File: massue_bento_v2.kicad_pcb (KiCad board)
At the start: 2 copper layers, 100 x 21 mm, 69 parts, among them K1 CONN_3, K2 CONN_3, K3 CONN_3, P1 TST, P10 CONN_1, P11 TST, P12 TST, P13 TST, P14 TST, P15 TST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

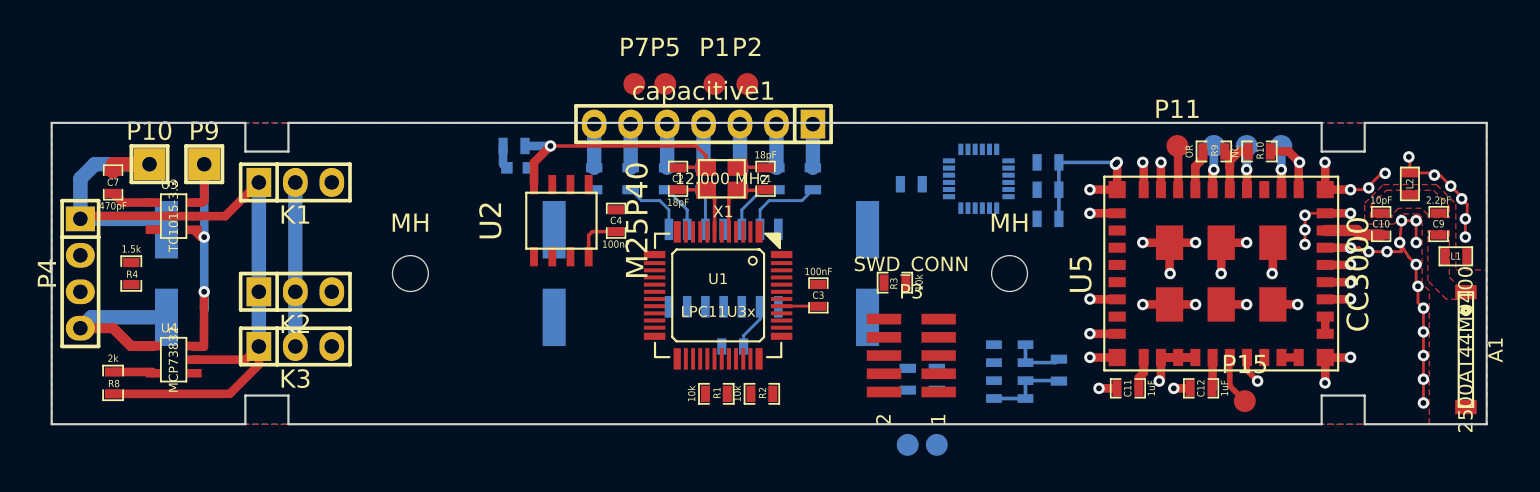
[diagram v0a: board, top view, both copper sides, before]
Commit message: New: first routing for almost all signals
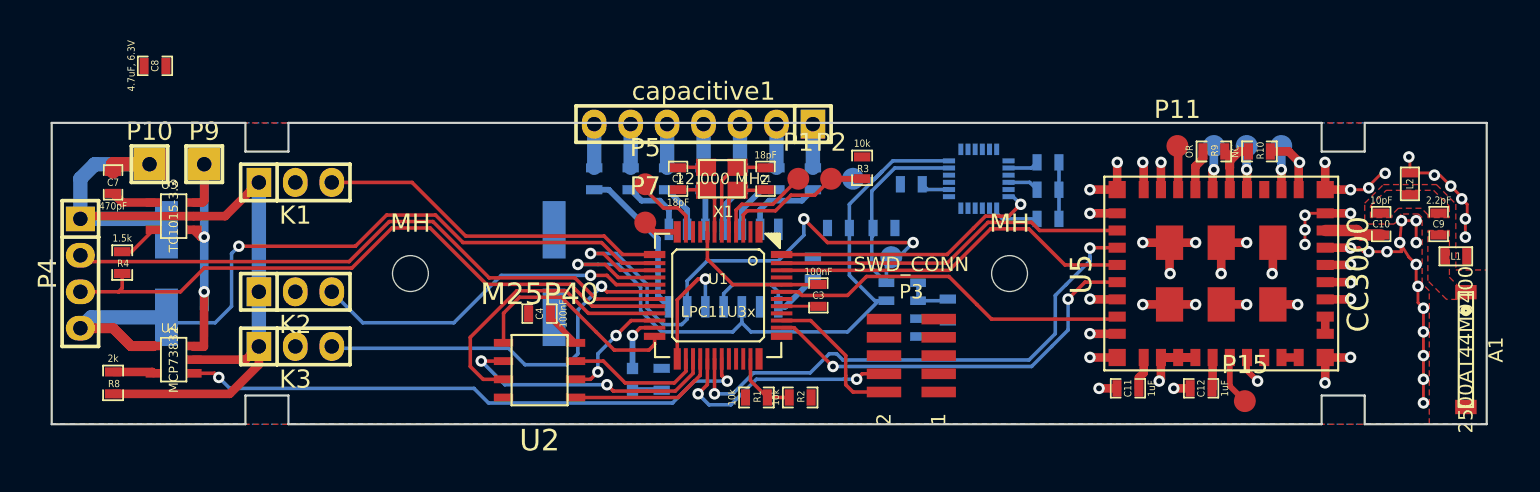
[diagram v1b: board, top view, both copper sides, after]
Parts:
- C8: value 220uF, 6.3V -> 4.7uF, 6.3V; footprint Capacitors_SMD:c_elec_8x6.7 -> SMD_Packages:SM0603_Capa; moved to F.Cu
- U7: footprint Tom:LGA -> LGA
- moved C8 51.7 mm to (106.2, 95.5), turned to 0 degrees
- moved P8 19.4 mm to (154.8, 103.4)
- moved R7 19.2 mm to (141.5, 117.4), turned to 90 degrees
- moved D1 16.8 mm to (139.5, 117.4), turned to 270 degrees
- moved P6 13.1 mm to (157.5, 108.9)
- moved R6 12.6 mm to (153.8, 106.8), turned to 0 degrees
- moved R5 10.7 mm to (157.0, 106.8), turned to 180 degrees
- moved U2 10.5 mm to (133.0, 116.7), turned to 0 degrees
- moved P7 9.68 mm to (140.4, 106.4)
- moved P1 8.82 mm to (151.0, 103.4)
- moved P2 8.82 mm to (153.3, 103.4)
- moved C18 8.81 mm to (161.4, 112.5)
- moved U8 8.65 mm to (158.3, 112.5)
- moved C4 8.39 mm to (133.0, 112.8), turned to 180 degrees
- moved R3 8.32 mm to (155.5, 102.6), turned to 270 degrees
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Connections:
- net Net-(D1-Pad1) renamed /ONBOARD_LED
- K1 pad 2: +3.3V -> VBAT
- K2 pad 2: +3.3V -> VBAT
- K3 pad 2: +3.3V -> VBAT
- U1 pad 13: /FLASH_SCK -> /LED1
- U1 pad 17: /sensors/MPU9150_INT -> /LED2
- U1 pad 18: (no net) -> /LED3
- U1 pad 21: (no net) -> /FLASH_WRITE
- U1 pad 22: (no net) -> /FLASH_SCK
- U1 pad 24: (no net) -> /FLASH_CS
- U1 pad 26: /FLASH_MISO -> /FLASH_HOLD
- U1 pad 27: /RF/CC3000_SPI_DOUT -> /FLASH_MISO
- U1 pad 28: /RF/CC3000_SPI_DIN -> /FLASH_MOSI
- U1 pad 30: /LED2 -> /RF/CC3000_SPI_DOUT
- U1 pad 31: /RF/CC3000_SPI_CLK -> /power/LIPO_CHRG_STAT
- U1 pad 32: /BATT_MON -> (no net)
- U1 pad 33: /power/LIPO_CHRG_STAT -> (no net)
- U1 pad 35: (no net) -> /BATT_MON
- U1 pad 36: /FLASH_CS -> (no net)
- U1 pad 37: /FLASH_WRITE -> (no net)
- U1 pad 38: /FLASH_MOSI -> /RF/CC3000_SPI_DIN
- U1 pad 40: /LED1 -> (no net)
- U1 pad 42: /LED3 -> (no net)
- U1 pad 43: /FLASH_HOLD -> /RF/CC3000_SPI_CLK
- U1 pad 48: (no net) -> /sensors/MPU9150_INT
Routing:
- net /sensors/SCL: track 0.00 -> 54.5 mm, vias 0 -> 3
- net /sensors/SDA: track 0.00 -> 51.4 mm, vias 0 -> 1
- net /USB_DP: track 0.00 -> 45.5 mm
- net /USB_DN: track 0.00 -> 43.6 mm
- net +5V_USB: track 15.3 -> 56.1 mm, vias 0 -> 1
- net /power/LIPO_CHRG_STAT: track 0.00 -> 40.4 mm, vias 0 -> 2
- net /RF/CC3000_SPI_DOUT: track 0.00 -> 37.2 mm, vias 0 -> 2
- net GND: track 205.6 -> 173.9 mm, vias 58 -> 56
- net /RF/CC3000_SPI_DIN: track 0.00 -> 28.2 mm, vias 0 -> 2
- net /LED3: track 0.00 -> 27.2 mm, vias 0 -> 1
- net /RF/CC3000_SPI_IRQ: track 0.00 -> 25.6 mm
- net /RF/CC3000_SPI_CLK: track 0.00 -> 25.3 mm
- net /LED2: track 0.00 -> 25.0 mm, vias 0 -> 1
- net /RF/CC3000_SPI_CS: track 0.00 -> 24.8 mm
- net /LED1: track 0.00 -> 24.6 mm
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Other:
- net class Default: clearance 0.2 -> 0.18
- net class POWER: clearance 0.3 -> 0.18
- rule trace_clearance: 0.2 -> 0.18
- board text added: "ToDo : C8 en sortie du rég 3V3"

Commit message: Finished routing of signals, re-organization of power
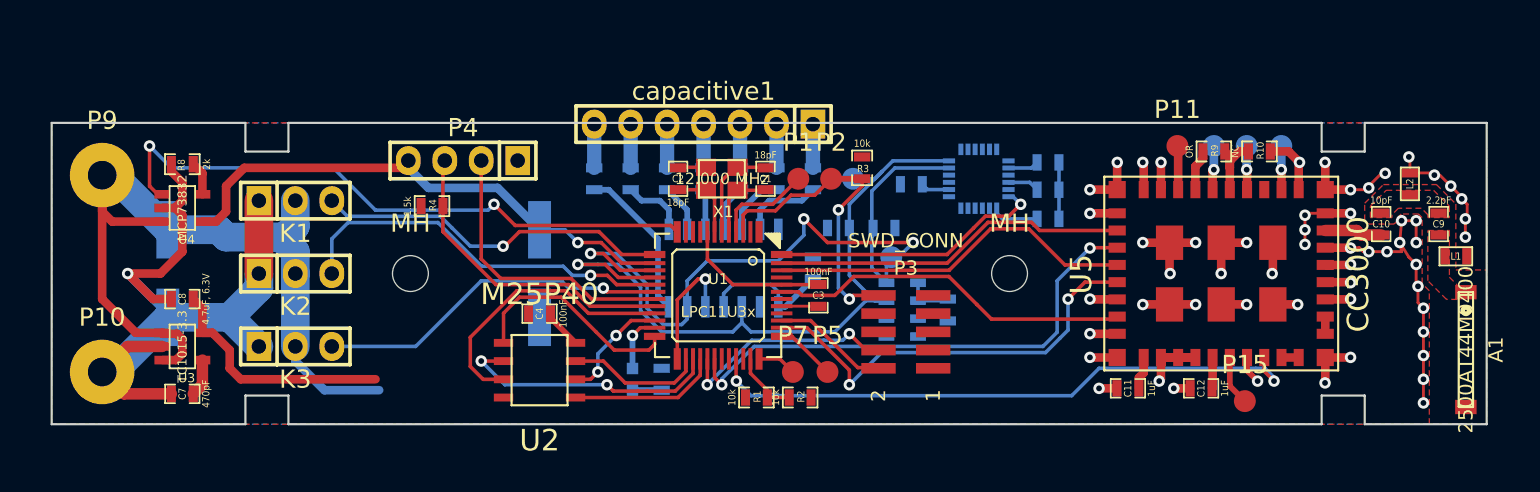
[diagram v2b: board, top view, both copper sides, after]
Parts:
- P10, P9: footprint Socket_Strips:Socket_Strip_Straight_1x01 -> Wire_Pads:SolderWirePad_single_2mmDrill
- U7: footprint LGA -> Tom:LGA
- moved P4 27.8 mm to (127.7, 102.1), turned to 0 degrees
- moved C5 26.9 mm to (107.1, 110.0), turned to 90 degrees
- moved C6 26.0 mm to (133.0, 110.0), turned to 90 degrees
- moved R4 21.9 mm to (125.5, 105.3), turned to 0 degrees
- moved P5 18.2 mm to (153.1, 116.9)
- moved C8 16.4 mm to (108.1, 111.8), turned to 180 degrees
- moved R8 16.0 mm to (108.1, 102.4), turned to 180 degrees
- moved C7 15.5 mm to (108.1, 118.4), turned to 180 degrees
- moved P10 14.8 mm to (102.5, 116.9)
- moved P7 14.6 mm to (150.7, 116.9)
- moved U4 10.6 mm to (108.1, 105.4), turned to 270 degrees
- moved U3 9.10 mm to (108.1, 115.1), turned to 270 degrees
- moved P9 7.15 mm to (102.5, 103.1)
- moved P3 1.69 mm to (158.5, 114.1)
- moved K1 1.27 mm to (116.0, 104.9)
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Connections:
- U1 pad 11: /RX -> (no net)
- U1 pad 12: /TX -> /power/LIPO_CHRG_STAT
- U1 pad 31: /power/LIPO_CHRG_STAT -> (no net)
- U1 pad 33: (no net) -> /RF/CC3000_SW_EN
- U1 pad 36: (no net) -> /TX
- U1 pad 37: (no net) -> /RX
- U1 pad 45: /RF/CC3000_SW_EN -> (no net)
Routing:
- net /RF/CC3000_SW_EN: track 0.00 -> 42.7 mm, vias 0 -> 2
- net VBAT: track 22.6 -> 62.2 mm, vias 2 -> 0
- net /USB_DP: track 45.5 -> 21.9 mm
- net /USB_DN: track 43.6 -> 20.1 mm
- net +5V_USB: track 56.1 -> 37.6 mm
- net +3.3V: track 36.4 -> 50.4 mm
- net /RESET: track 10.5 -> 22.0 mm, vias 0 -> 2
- net GND: track 173.9 -> 167.9 mm, vias 56 -> 57
- net /power/LIPO_CHRG_STAT: track 40.4 -> 43.6 mm
- net /LED3: track 27.2 -> 24.9 mm
- net /SWDIO: track 10.4 -> 8.16 mm
- net /LED2: track 25.0 -> 27.2 mm
- net /RF/CC3000_SPI_DIN: track 28.2 -> 29.8 mm
- net /RF/CC3000_SPI_DOUT: track 37.2 -> 35.9 mm
- net /SWCLK: track 16.9 -> 15.7 mm
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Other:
- board text removed: "ToDo : C8 en sortie du rég 3V3"

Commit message: new : power ehencement
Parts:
- moved P5 0.51 mm to (152.6, 116.9)
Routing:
- net GND: track 167.9 -> 332.2 mm, vias 57 -> 65
- net +3.3V: track 50.4 -> 157.0 mm, vias 0 -> 7
- net VBAT: track 62.2 -> 121.9 mm, vias 0 -> 2
- net /sensors/SCL: track 54.5 -> 53.0 mm
- net /RF/CC3000_SPI_DIN: track 29.8 -> 28.8 mm
- net /RX: track 4.22 -> 3.38 mm

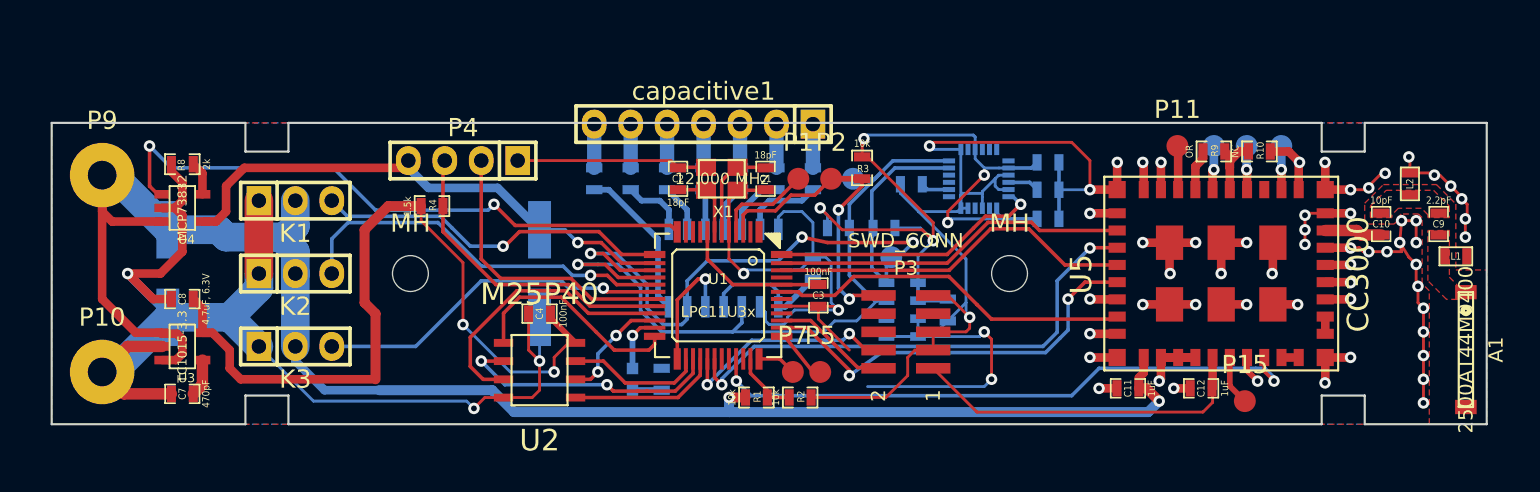
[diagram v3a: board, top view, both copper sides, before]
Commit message: New: first complete routing, no more unconnected nets
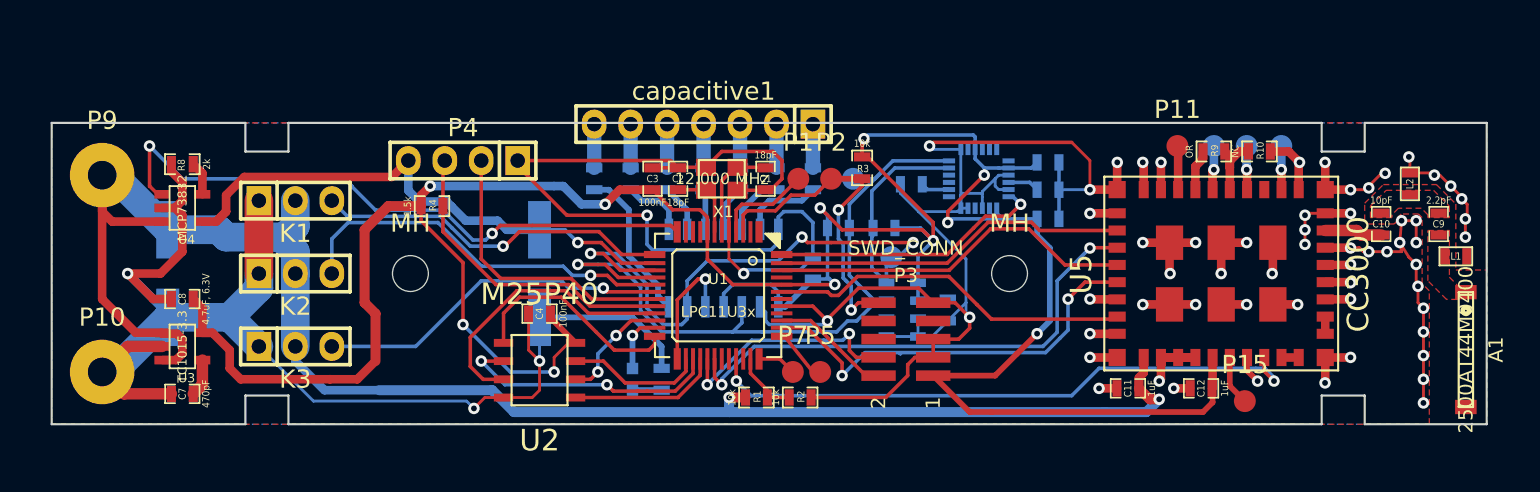
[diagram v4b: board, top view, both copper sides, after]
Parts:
- moved C3 14.1 mm to (140.9, 103.4), turned to 90 degrees
- moved P3 0.51 mm to (158.5, 114.6)
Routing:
- net +3.3V: track 157.0 -> 204.0 mm, vias 7 -> 11
- net GND: track 332.2 -> 356.3 mm, vias 65 -> 64
- net +5V_USB: track 37.6 -> 40.5 mm
- net /RESET: track 22.0 -> 24.0 mm
- net /SWCLK: track 15.7 -> 17.5 mm
- net /RF/CC3000_SPI_DIN: track 28.8 -> 29.4 mm
- net /power/LIPO_CHRG_STAT: track 43.6 -> 44.1 mm
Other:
- net class Default: trace_width 0.2 -> 0.25

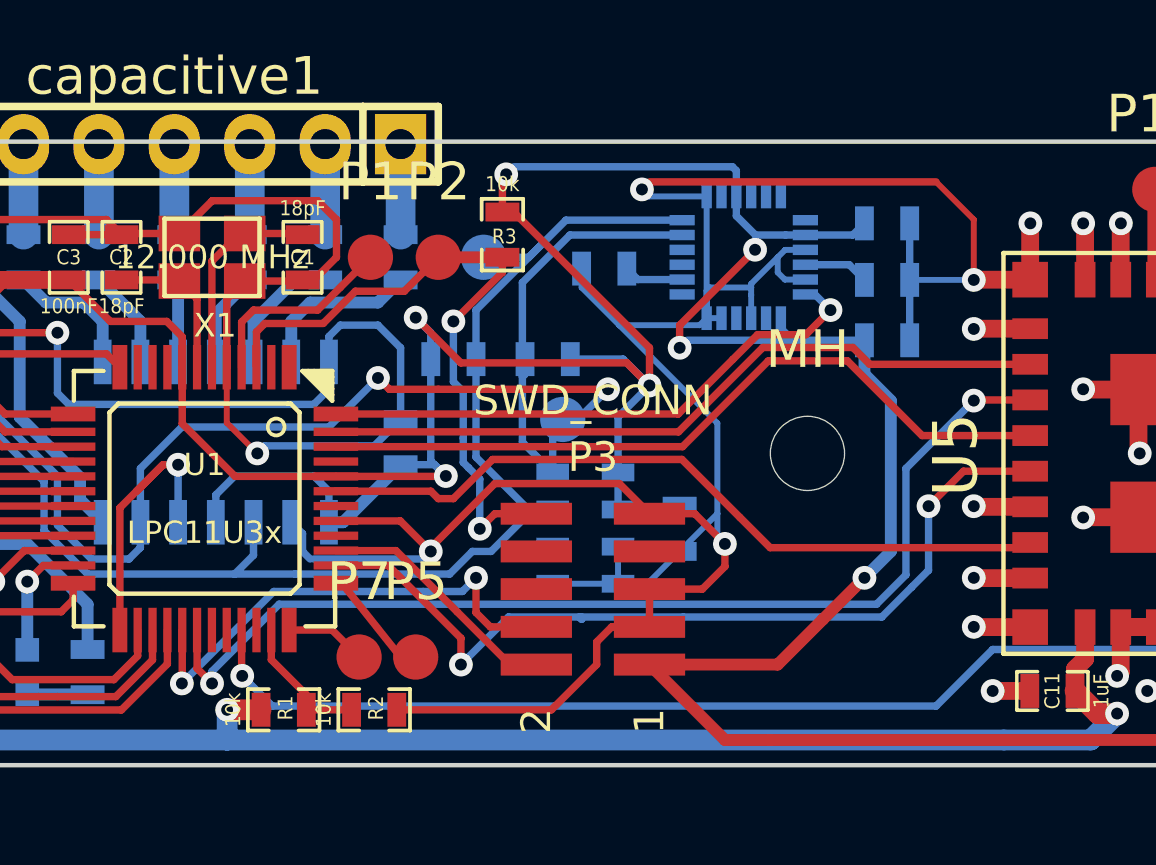
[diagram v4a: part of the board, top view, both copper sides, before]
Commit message: Changed MS5607 altimeter for MPL3115A2
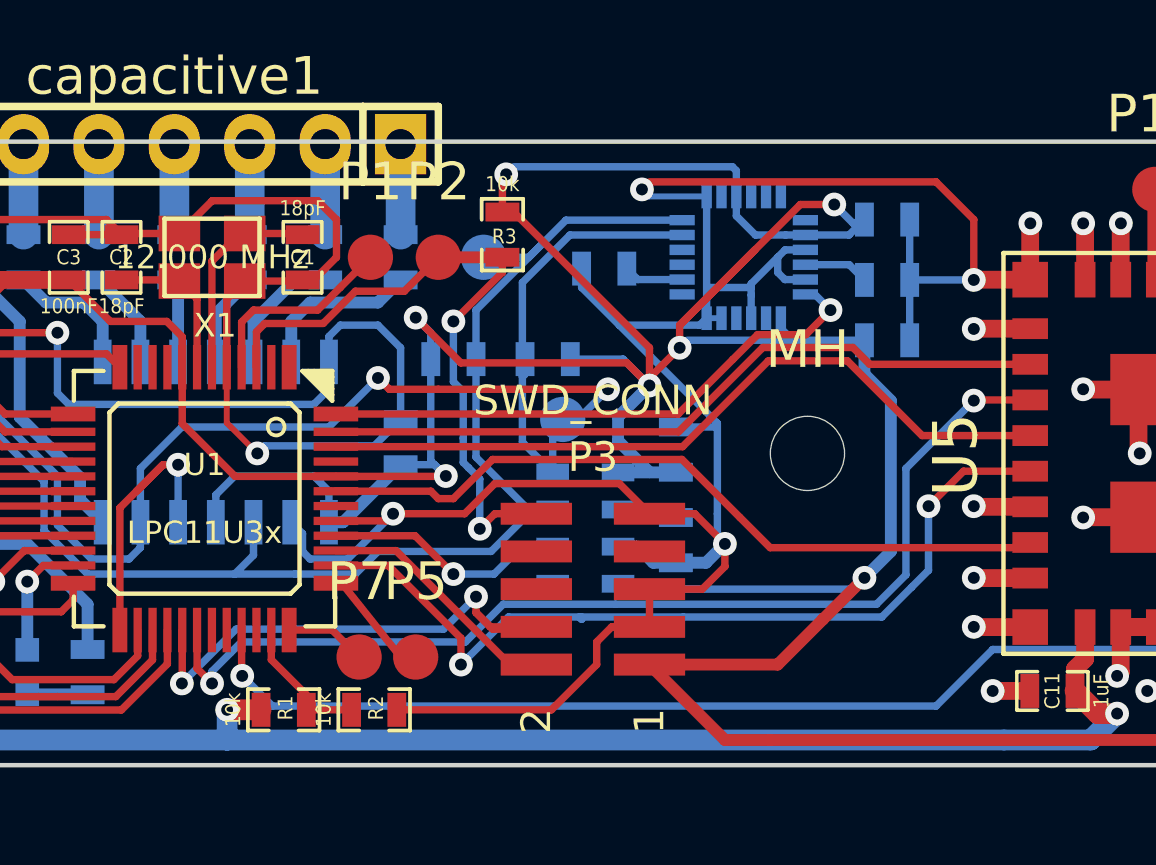
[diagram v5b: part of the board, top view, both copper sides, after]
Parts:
- added C19: 100nF, SMD_Packages:SM0603_Capa, B.Cu at (161.3, 112.9)
- U8: value MS5607 -> MPL3115A2; footprint Tom:MS5607 Package -> Tom:LGA8
- moved C18 2.67 mm to (161.3, 109.9), turned to 90 degrees
- moved C14 0.13 mm to (168.4, 102.1)
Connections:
- U1 pad 40: (no net) -> /sensors/MPL3115_INT
- U8 pad 2: +3.3V -> Net-(C19-Pad1)
- U8 pad 4: GND -> +3.3V
- U8 pad 5: GND -> (no net)
- U8 pad 6: (no net) -> /sensors/MPL3115_INT
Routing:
- net +3.3V: track 204.0 -> 221.9 mm
- net /sensors/MPL3115_INT: track 0.00 -> 8.22 mm, vias 0 -> 1
- net GND: track 356.3 -> 352.5 mm
- net Net-(C19-Pad1): track 0.00 -> 2.44 mm
- net /SWCLK: track 17.5 -> 18.9 mm

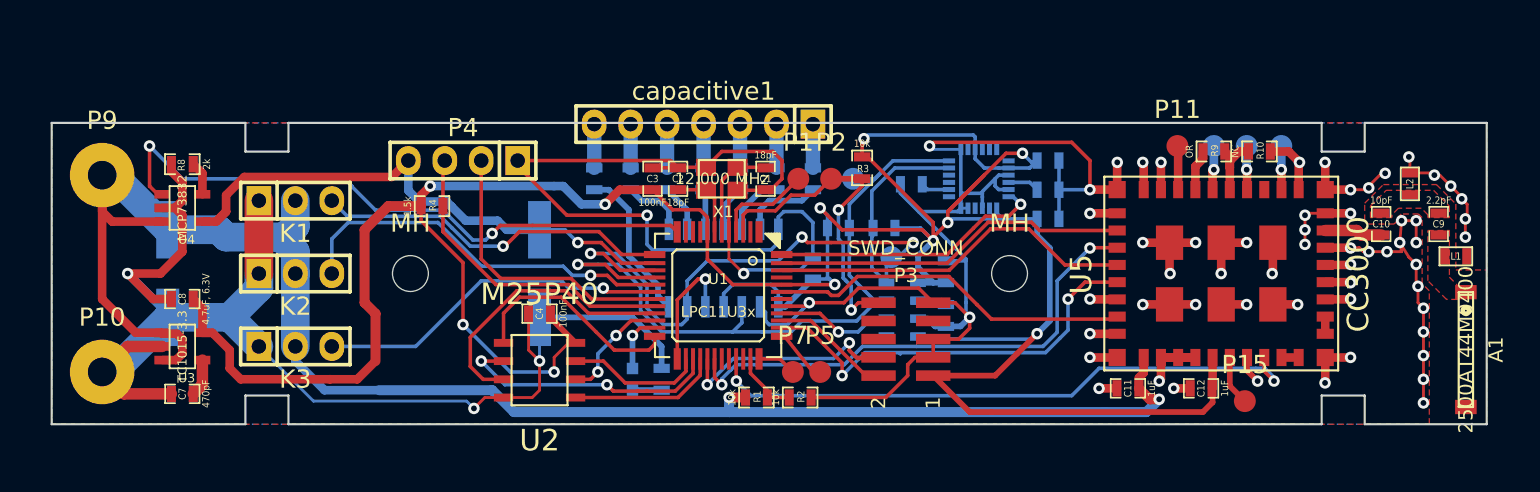
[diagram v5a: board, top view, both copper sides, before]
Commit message: Clean: additionnal ground vias, fixed USB differential signals length, add some labels
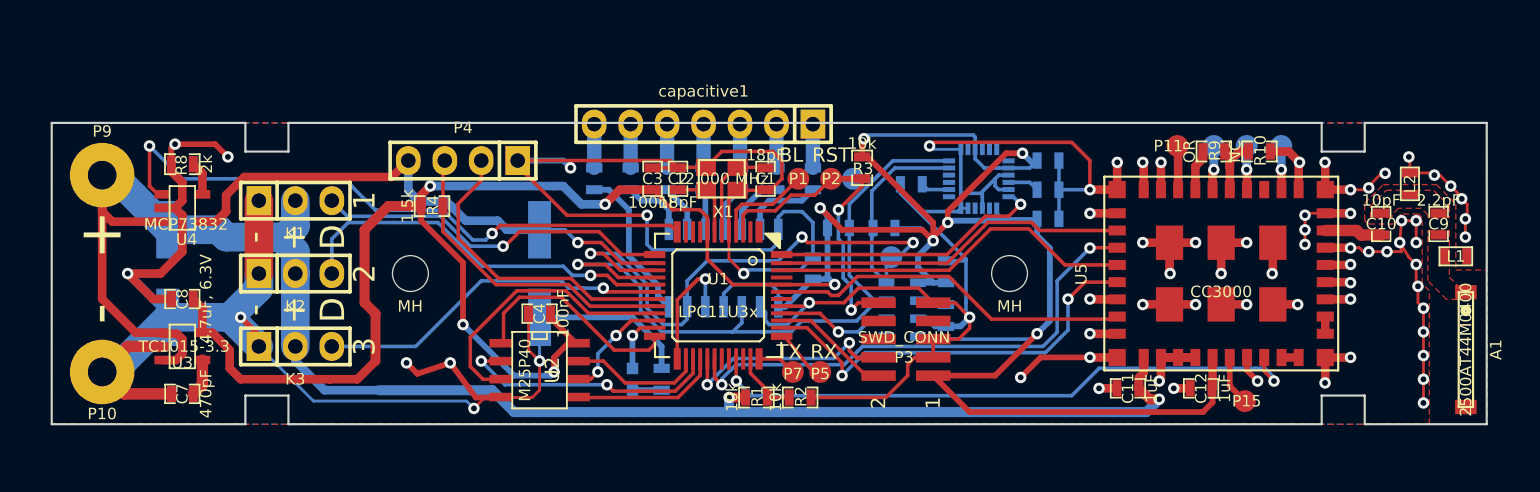
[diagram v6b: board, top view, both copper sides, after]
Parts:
- U2: footprint Tom:SO8N -> SOIC_Packages:SOIC-8_N
- turned U2 to 270 degrees
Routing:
- net GND: track 352.5 -> 380.6 mm, vias 64 -> 71
- net +3.3V: track 221.9 -> 224.5 mm
- net /USB_DN: track 20.1 -> 21.5 mm
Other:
- board text added: "+"
- board text added: "-"
- board text added: "- + D"
- board text added: "0"
- board text added: "1"
- board text added: "2"
- board text added: "3"
- board text added: "6"
- board text added: "BL"
- board text added: "GND D- D+ +5V"
- board text added: "RST"
- board text added: "RX"
- board text added: "SCL"
- board text added: "SDA"
- board text added: "TX"
- board text added: "USB"

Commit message: Added version label and logo
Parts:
- added G***: LOGO, Tom:Logo_Bento, B.Cu at (179.7, 108.6)
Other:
- board text added: "07/2014"
- board text added: "A. Meissonnier"
- board text added: "Massue Bento v2"
- board text added: "T. Magnier"

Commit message: Add X/Y label for IMU axes
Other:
- board text added: "X"
- board text added: "Y"
